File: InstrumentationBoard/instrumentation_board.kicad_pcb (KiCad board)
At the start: 2 copper layers, 65 x 104 mm, 59 parts, among them J1 Conn_01x02, J2 Conn_01x02, J3 Conn_01x02, J4 Conn_01x02, J5 Conn_01x02, Q1 TEMT6000X01, U1 GPS-ADAFRUIT746, U10 PI4ULS5V201TAEX, U11 PI4ULS5V201TAEX, U12 PI4ULS5V201TAEX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

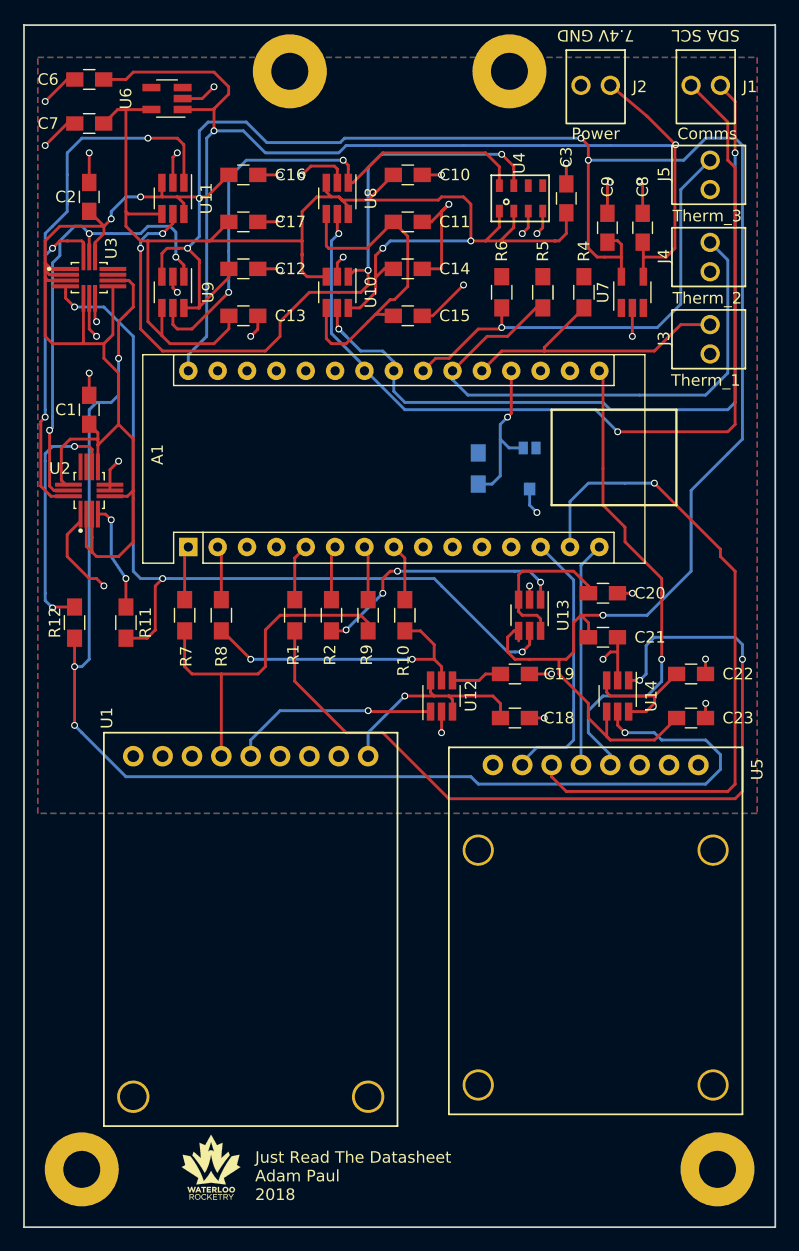
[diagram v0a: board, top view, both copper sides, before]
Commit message: Cleaned up files + Updated Footprints
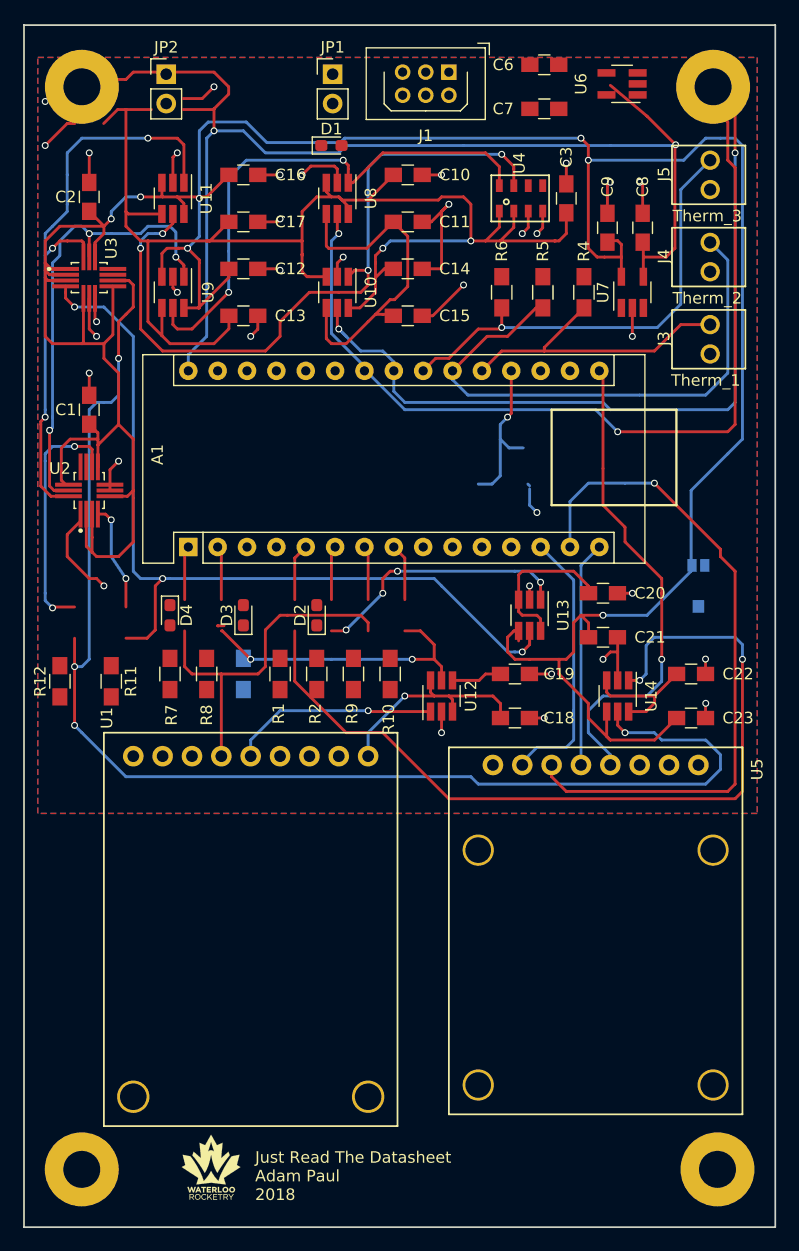
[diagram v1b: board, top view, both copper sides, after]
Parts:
- removed J2: Conn_01x02, molex:molex_kk_22-23-2021
- added D1: LED, Diode_SMD:D_0603_1608Metric_Pad1.05x0.95mm_HandSolder, F.Cu at (101.6, 58.4)
- added D2: LED, Diode_SMD:D_0603_1608Metric_Pad1.05x0.95mm_HandSolder, F.Cu at (100.3, 99.1)
- added D3: LED, Diode_SMD:D_0603_1608Metric_Pad1.05x0.95mm_HandSolder, F.Cu at (94.0, 99.1)
- added D4: LED, Diode_SMD:D_0603_1608Metric_Pad1.05x0.95mm_HandSolder, F.Cu at (87.6, 99.1)
- added JP1: Jumper, Connector_PinHeader_2.54mm:PinHeader_1x02_P2.54mm_Vertical, F.Cu at (101.7, 52.2)
- added JP2: Jumper, Connector_PinHeader_2.54mm:PinHeader_1x02_P2.54mm_Vertical, F.Cu at (87.3, 52.2)
- C6, C7: value 1uF -> C
- J1: value Conn_01x02 -> Conn_01x06; footprint molex:molex_kk_22-23-2021 -> Connector_Harwin:Harwin_LTek-Male_2x03_P2.00mm_Vertical
- R1, R2, R7: value 0 -> 120
- R3: value 10K -> 120
- U1: value GPS-ADAFRUIT746 -> LSM303AGR
- moved C6 39.4 mm to (120.0, 51.4)
- moved C7 39.4 mm to (120.0, 55.2)
- moved U6 39.4 mm to (126.7, 53.1)
- moved R3 27.0 mm to (94.0, 104.1), turned to 270 degrees
- moved J1 22.3 mm to (111.8, 52.1)
- moved REF** 18.0 mm to (80.0, 53.3)
- moved Q1 17.8 mm to (133.3, 96.5)
- moved REF** 17.7 mm to (134.6, 53.3)
- moved R11 5.24 mm to (82.5, 104.8)
- moved R12 5.24 mm to (78.1, 104.8)
- moved R7 5.24 mm to (87.6, 104.1)
- moved R9 5.24 mm to (103.5, 104.1)
- moved R1 5.24 mm to (97.2, 104.1)
- moved R10 5.24 mm to (106.7, 104.1)
- moved R2 5.24 mm to (100.3, 104.1)
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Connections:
- A1 pad 12: Net-(A1-Pad12) -> INIT_MAG
- A1 pad 30: 7.4V -> Net-(A1-Pad30)
- C6 pad 1: 7.4V -> Net-(C6-Pad1)
- C7 pad 1: 3V -> 1.8V
- J1 pad 1: SDA_5V -> GND
- J1 pad 2: SCL_5V -> 1.8V
- R1 pad 1: INT1_5V -> Net-(D1-Pad2)
- R1 pad 2: Net-(A1-Pad5) -> 1.8V
- R11 pad 1: Net-(R11-Pad1) -> INT0_1.8V
- R11 pad 2: INT0_1.8V -> Net-(R11-Pad2)
- R12 pad 1: INT1_1.8V -> Net-(R12-Pad1)
- R12 pad 2: Net-(R12-Pad2) -> INT1_1.8V
- R2 pad 1: INT0_5V -> Net-(D2-Pad2)
- R2 pad 2: Net-(A1-Pad6) -> 3V
- R3 pad 1: SIG -> Net-(D3-Pad2)
- R3 pad 2: GND -> 5V
- R7 pad 1: GPS_IN -> Net-(D4-Pad2)
- R7 pad 2: Net-(A1-Pad1) -> Net-(A1-Pad11)
- U1 pad 1: Net-(U1-Pad1) -> SCL_1.8V
- U1 pad 2: 5V -> 1.8V
- U1 pad 3: GND -> 1.8V
- U1 pad 4: GPS_IN -> SDA_1.8V
- U1 pad 5: /ICShifter7/A -> Net-(C6-Pad1)
- U1 pad 6: Net-(U1-Pad6) -> GND
- U1 pad 7: Net-(U1-Pad7) -> INIT_MAG
- U1 pad 8: Net-(U1-Pad8) -> GND
- U1 pad 9: /ICShifter7/VccA -> 1.8V
- U2 pad 4: Net-(R11-Pad1) -> Net-(R11-Pad2)
- U2 pad 9: Net-(R12-Pad2) -> Net-(R12-Pad1)
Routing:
- net GPS_IN: track 31.3 -> 0.00 mm
- net SDA_1.8V: track 51.8 -> 83.1 mm
- net Net-(R12-Pad2): track 21.5 -> 0.00 mm, vias 2 -> 0
- net Net-(R12-Pad1): track 0.00 -> 21.5 mm, vias 0 -> 2
- net Net-(R11-Pad2): track 0.00 -> 9.28 mm, vias 0 -> 2
- net Net-(R11-Pad1): track 9.28 -> 0.00 mm, vias 2 -> 0
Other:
- board text removed: "7.4V GND"
- board text removed: "Comms"
- board text removed: "Power"
- board text removed: "SDA SCL"

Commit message: Updated Schematics + Started Baseboard PCB
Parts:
- added C4: C, Capacitor_SMD:C_0805_2012Metric_Pad1.15x1.40mm_HandSolder, F.Cu at (125.7, 58.4)
- added C5: C, Capacitor_SMD:C_0805_2012Metric_Pad1.15x1.40mm_HandSolder, F.Cu at (130.5, 58.4)
- U1: footprint adafruit:gps746 -> Package_LGA:LGA-12_2x2mm_P0.5mm
- moved U1 52.1 mm to (94.0, 57.1), turned to 0 degrees
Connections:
- net /Sheet5ABF9899/THERM_OUT renamed /Thermistor 2/THERM_OUT
- net /Sheet5ABF9899_2/THERM_OUT renamed /Thermistor/THERM_OUT
- net /Sheet5ABF9899_3/THERM_OUT renamed /Thermistor 3/THERM_OUT
